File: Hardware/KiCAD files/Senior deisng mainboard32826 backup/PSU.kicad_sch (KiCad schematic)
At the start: 5 parts, among them U8 TPS54231DR

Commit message: Schematic adjustments made prior to initial submission to Chan thursday
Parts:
- removed D1: 650mV, imported schems:SOD-123HE, symbol imported schems-eagle-import:FSV360FPFSV360FP
- removed GND1, GND2: WB_GND, imported schems:WB_GND, symbol imported schems-eagle-import:WB_GNDWB_GND
- removed L1: 15uH, imported schems:DR1040, symbol imported schems-eagle-import:DR1040-150-RDR1040-150-R
- removed U8: TPS54231DR, imported schems:D0008A, symbol imported schems-eagle-import:TPS54231DRTPS54231DR
- added C10: C_Generic 1mF, 300mOhm ESR, symbol PCM_Capacitor_AKL:C_Generic
- added C11: C_Generic 220 uF, 180 mohm ESR qty=2, symbol PCM_Capacitor_AKL:C_Generic
- added C12: C_Generic 470 uF, 300mOhm ESR, symbol PCM_Capacitor_AKL:C_Generic
- added C9: C_Generic 68 uF, 340mohm ESR qty = 3, symbol PCM_Capacitor_AKL:C_Generic
- added D1, D2: SK34A, PCM_SparkFun-Semiconductor-Standard:SMA, symbol PCM_SparkFun-DiscreteSemi:D_Schottky_3A_40V_0.55V
- added L1: L,IEC, 100 uH, 8.25 ESR, symbol PCM_Generic:L,IEC
- added L2: L,IEC, 150 uH, 12.5 ESR, symbol PCM_Generic:L,IEC
- added U2, U3: LM2576HVT-5.0/LF02, T05A_TEX, symbol LM2576 regulator:LM2576HVT-5.0_LF02
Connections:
- new net: D1.1 (K), L1.1 (+), U2.2 (OUT)
- new net: D2.1 (K), L2.1 (+), U3.2 (OUT)
- new net +24V: C11.1, C9.1, U2.1 (VIN), U3.1 (VIN)
- new net +3.3V: C10.1, C12.1, L1.2 (-), L2.2 (-), U2.4 (FB), U3.4 (FB)
- new net GND: C10.2, C11.2, C12.2, C9.2, D1.2 (A), D2.2 (A), U2.3 (GND), U2.5 (*ON/OFF), U3.3 (GND), U3.5 (*ON/OFF)
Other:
- note added: "+3.3V regulator"
- note added: "+5V regulator"
- note removed: "5V regulator"
- note removed: "Note: I have the report with all the compnents from webench. I need to find and place the parts since they error in kicad"

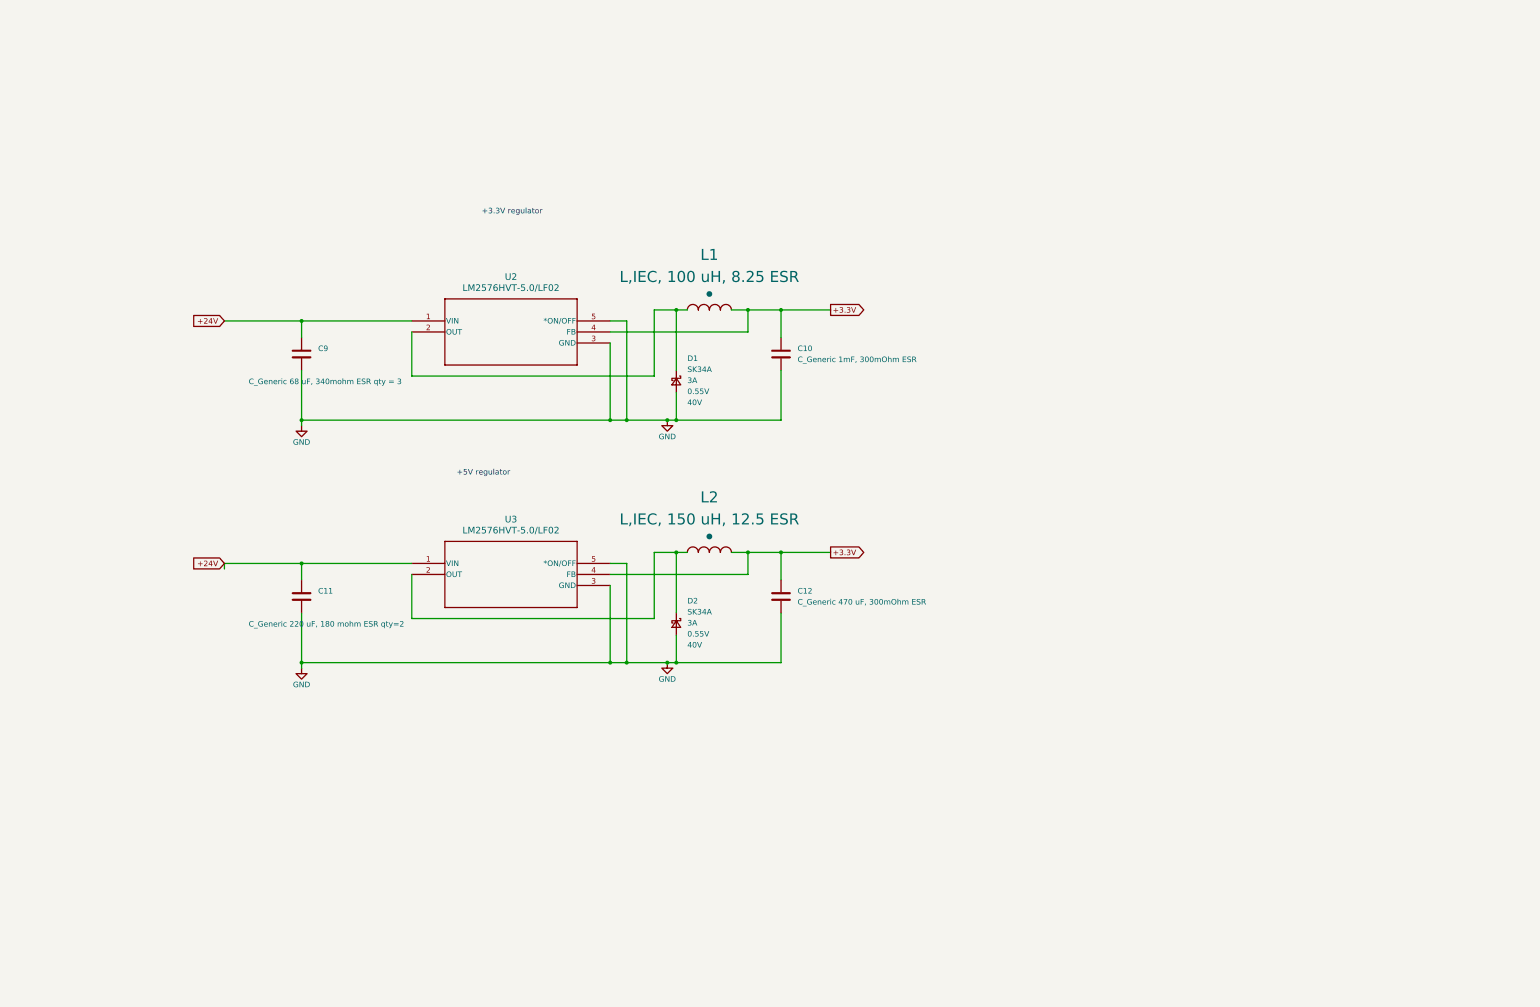
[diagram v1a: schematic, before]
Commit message: IO pull resistors, Motor driver V1, LCD communication
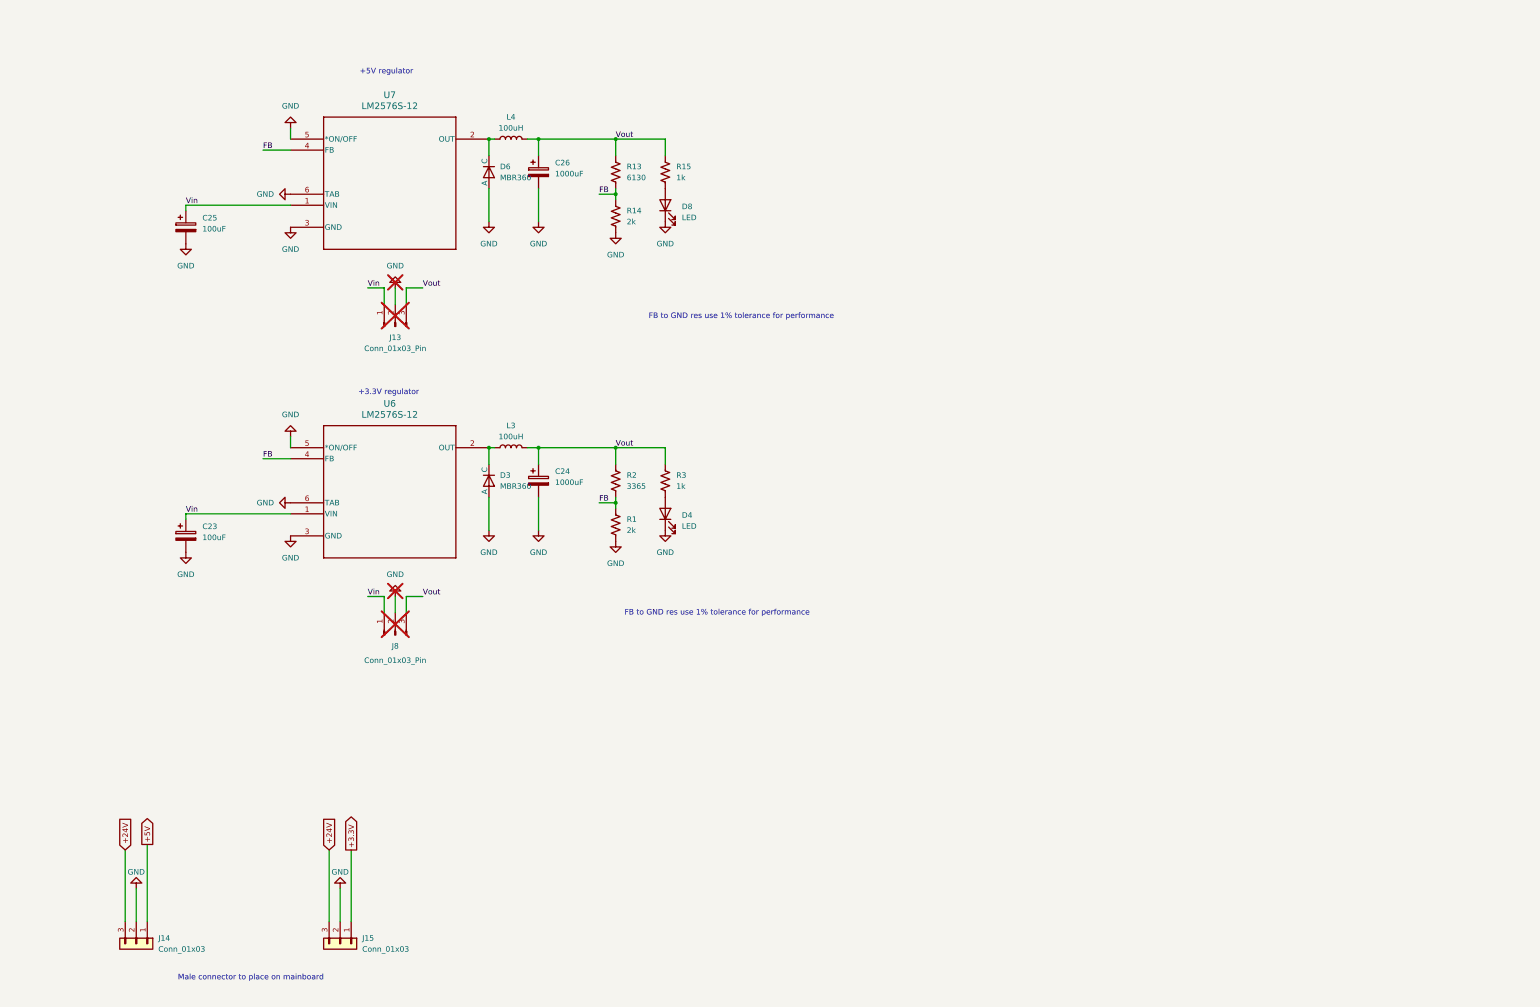
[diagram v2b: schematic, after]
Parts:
- removed C10: C_Generic 1mF, 300mOhm ESR, symbol PCM_Capacitor_AKL:C_Generic
- removed C11: C_Generic 220 uF, 180 mohm ESR qty=2, symbol PCM_Capacitor_AKL:C_Generic
- removed C12: C_Generic 470 uF, 300mOhm ESR, symbol PCM_Capacitor_AKL:C_Generic
- removed C9: C_Generic 68 uF, 340mohm ESR qty = 3, symbol PCM_Capacitor_AKL:C_Generic
- removed D1, D2: SK34A, PCM_SparkFun-Semiconductor-Standard:SMA, symbol PCM_SparkFun-DiscreteSemi:D_Schottky_3A_40V_0.55V
- removed L1: L,IEC, 100 uH, 8.25 ESR, symbol PCM_Generic:L,IEC
- removed L2: L,IEC, 150 uH, 12.5 ESR, symbol PCM_Generic:L,IEC
- removed U2, U3: LM2576HVT-5.0/LF02, T05A_TEX, symbol LM2576 regulator:LM2576HVT-5.0_LF02
- added C23, C25: 100uF, symbol Device:C_Polarized
- added C24, C26: 1000uF, symbol Device:C_Polarized
- added D3, D6: MBR360, symbol MBR360:Diode
- added D4, D8: LED, symbol Device:LED
- added J13, J8: Conn_01x03_Pin, Connector_PinHeader_1.00mm:PinHeader_1x03_P1.00mm_Vertical, symbol Connector:Conn_01x03_Pin
- added J14, J15: Conn_01x03, PCM_SparkFun-Connector:1x03_P2.54mm, symbol PCM_SparkFun-Connector:Conn_01x03_P2.54mm
- added L3, L4: 100uH, Inductor_SMD:L_1206_3216Metric_Pad1.22x1.90mm_HandSolder, symbol Device:L
- added R1, R14: 2k, symbol Device:R_US
- added R13: 6130, symbol Device:R_US
- added R15, R3: 1k, Resistor_SMD:R_1206_3216Metric_Pad1.30x1.75mm_HandSolder, symbol Device:R_US
- added R2: 3365, symbol Device:R_US
- added U6, U7: LM2576S-12, TS5B_TEX, symbol LM2576ADJ:LM2576S-12
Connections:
- net +24V: now also J14.3 (Pin_3), J15.3 (Pin_3)
- net +3.3V: now also J15.1 (Pin_1)
- net GND: now also C23.2, C24.2, C25.2, C26.2, D3.1 (A), D4.1 (K), D6.1 (A), D8.1 (K), J13.2 (Pin_2), J14.2 (Pin_2), J15.2 (Pin_2), J8.2 (Pin_2), R1.2, R14.2, U6.3 (GND), U6.5 (*ON/OFF), U6.6 (TAB), U7.3 (GND), U7.5 (*ON/OFF), U7.6 (TAB)
- new net: D3.2 (C), L3.1, U6.2 (OUT)
- new net: D4.2 (A), R3.2
- new net: D6.2 (C), L4.1, U7.2 (OUT)
- new net: D8.2 (A), R15.2
- new net +5V: J14.1 (Pin_1)
- new net FB: R1.1, R13.2, R14.1, R2.2, U6.4 (FB), U7.4 (FB)
- new net Vin: C23.1, C25.1, J13.1 (Pin_1), J8.1 (Pin_1), U6.1 (VIN), U7.1 (VIN)
- new net Vout: C24.1, C26.1, J13.3 (Pin_3), J8.3 (Pin_3), L3.2, L4.2, R13.1, R15.1, R2.1, R3.1
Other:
- note added: "FB to GND res use 1% tolerance for performance"
- note added: "Male connector to place on mainboard"

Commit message: 1.1, devices have been cleaned up
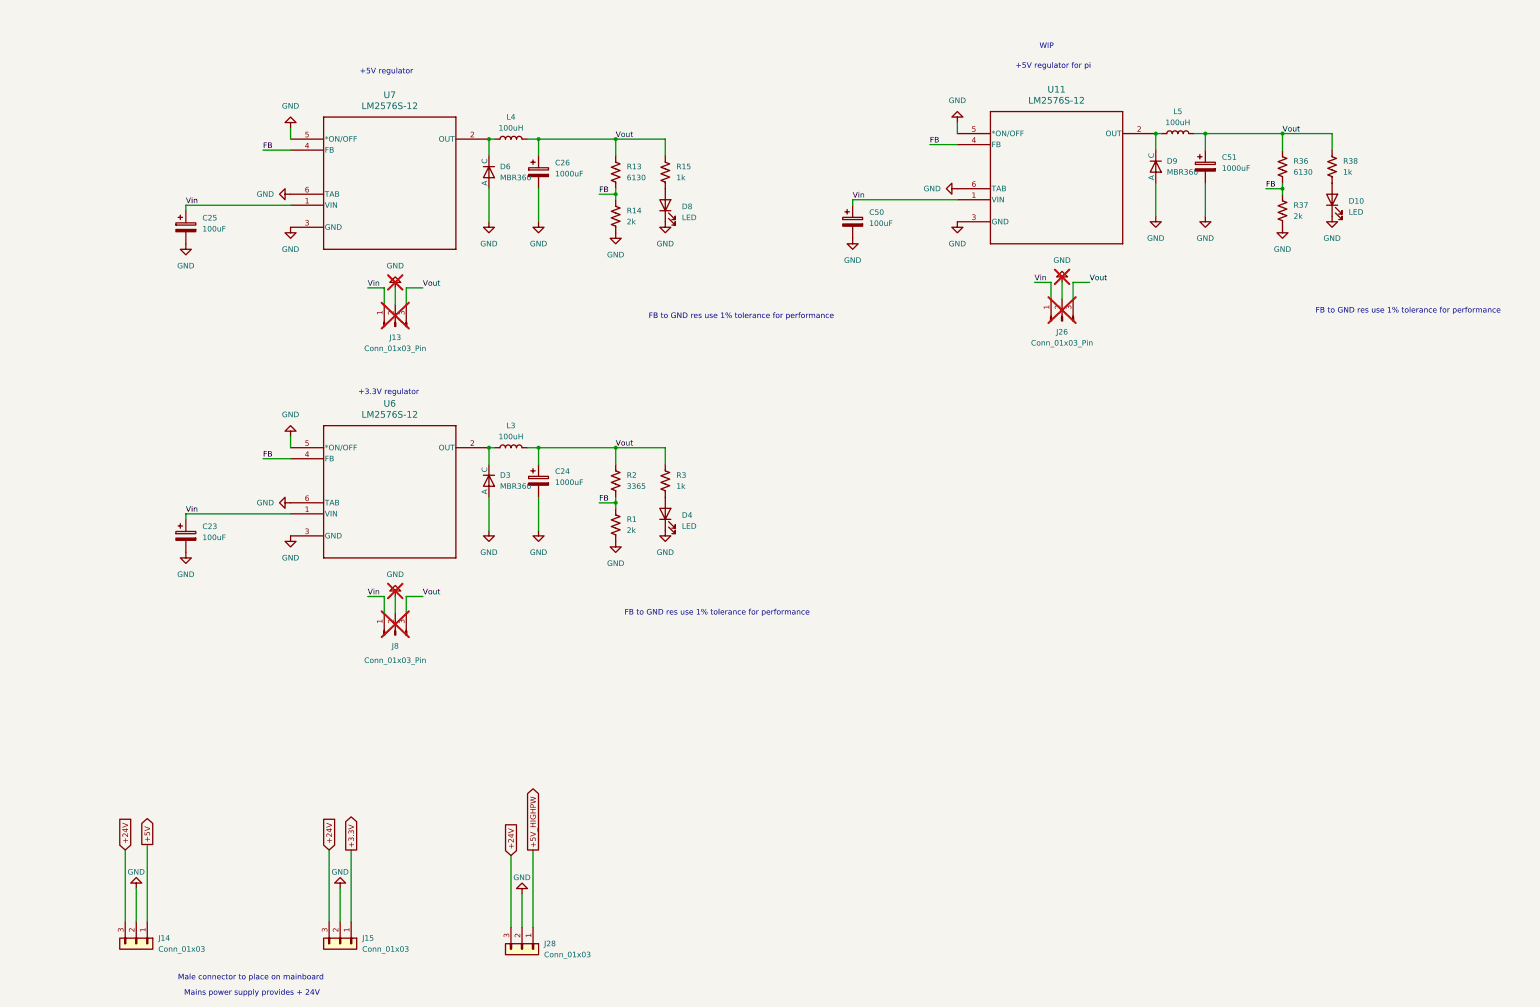
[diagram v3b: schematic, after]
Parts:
- added C50: 100uF, symbol Device:C_Polarized
- added C51: 1000uF, symbol Device:C_Polarized
- added D10: LED, symbol Device:LED
- added D9: MBR360, symbol MBR360:Diode
- added J26: Conn_01x03_Pin, Connector_PinHeader_1.00mm:PinHeader_1x03_P1.00mm_Vertical, symbol Connector:Conn_01x03_Pin
- added J28: Conn_01x03, PCM_SparkFun-Connector:1x03_P2.54mm, symbol PCM_SparkFun-Connector:Conn_01x03_P2.54mm
- added L5: 100uH, Inductor_SMD:L_1206_3216Metric_Pad1.22x1.90mm_HandSolder, symbol Device:L
- added R36: 6130, symbol Device:R_US
- added R37: 2k, symbol Device:R_US
- added R38: 1k, Resistor_SMD:R_1206_3216Metric_Pad1.30x1.75mm_HandSolder, symbol Device:R_US
- added U11: LM2576S-12, TS5B_TEX, symbol LM2576ADJ:LM2576S-12
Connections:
- net +24V: now also J28.3 (Pin_3)
- net FB: now also R36.2, R37.1, U11.4 (FB)
- net GND: now also C50.2, C51.2, D10.1 (K), D9.1 (A), J26.2 (Pin_2), J28.2 (Pin_2), R37.2, U11.3 (GND), U11.5 (*ON/OFF), U11.6 (TAB)
- net Vin: now also C50.1, J26.1 (Pin_1), U11.1 (VIN)
- net Vout: now also C51.1, J26.3 (Pin_3), L5.2, R36.1, R38.1
- new net: D9.2 (C), L5.1, U11.2 (OUT)
- new net: D10.2 (A), R38.2
- new net +5V_HIGHPW: J28.1 (Pin_1)
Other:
- note added: "+5V regulator for pi"
- note added: "Mains power supply provides + 24V"
- note added: "WIP"

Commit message: swapping connectors and rewiring through the project.
we verified connections with the ender3. a few placeholders replaced.
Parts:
- C23, C24, C25, C26, C50, C51: footprint (none) -> Capacitor_SMD:CP_Elec_5x3
- D10, D4, D8: footprint (none) -> LED_SMD:LED_0603_1608Metric
- U11, U6, U7: footprint TS5B_TEX -> (none)
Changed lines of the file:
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@@
 			)
 		)
-		(property "Footprint" ""
+		(property "Footprint" "Capacitor_SMD:CP_Elec_5x3"
 			(at 206.7052 81.28 0)
 			(hide yes)
@@
 			)
 		)
-		(property "Footprint" ""
+		(property "Footprint" "Capacitor_SMD:CP_Elec_5x3"
 			(at 287.9852 68.58 0)
 			(hide yes)
@@
 			)
 		)
-		(property "Footprint" "TS5B_TEX"
+		(property "Footprint" ""
 			(at 229.87 57.15 0)
 			(hide yes)
@@
 			)
 		)
-		(property "Footprint" ""
+		(property "Footprint" "LED_SMD:LED_0603_1608Metric"
 			(at 162.56 144.78 0)
 			(hide yes)
@@
 			)
 		)
-		(property "Footprint" ""
+		(property "Footprint" "Capacitor_SMD:CP_Elec_5x3"
 			(at 134.3152 140.97 0)
 			(hide yes)
@@
 			)
 		)
-		(property "Footprint" "TS5B_TEX"
+		(property "Footprint" ""
 			(at 76.2 58.42 0)
 			(hide yes)
@@
 			)
 		)
-		(property "Footprint" ""
+		(property "Footprint" "LED_SMD:LED_0603_1608Metric"
 			(at 162.56 73.66 0)
 			(hide yes)
@@
 			)
 		)
-		(property "Footprint" ""
+		(property "Footprint" "Capacitor_SMD:CP_Elec_5x3"
 			(at 53.0352 153.67 0)
 			(hide yes)
@@
 			)
 		)
-		(property "Footprint" ""
+		(property "Footprint" "LED_SMD:LED_0603_1608Metric"
 			(at 316.23 72.39 0)
 			(hide yes)
@@
 			)
 		)
-		(property "Footprint" ""
+		(property "Footprint" "Capacitor_SMD:CP_Elec_5x3"
 			(at 134.3152 69.85 0)
 			(hide yes)
@@
 			)
 		)
-		(property "Footprint" "TS5B_TEX"
+		(property "Footprint" ""
 			(at 76.2 129.54 0)
 			(hide yes)
@@
 			)
 		)
-		(property "Footprint" ""
+		(property "Footprint" "Capacitor_SMD:CP_Elec_5x3"
 			(at 53.0352 82.55 0)
 			(hide yes)
